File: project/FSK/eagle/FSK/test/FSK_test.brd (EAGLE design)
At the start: 173 x 74 mm, 31 parts, among them IC1 74AUC1G32DCK, X1 SMA-142-0711-821/826, X2 SMA-142-0711-821/826, X3 SMA-142-0711-821/826, X4 SMA-142-0711-821/826, X5 SMA-142-0711-821/826, X6 22-23-2021

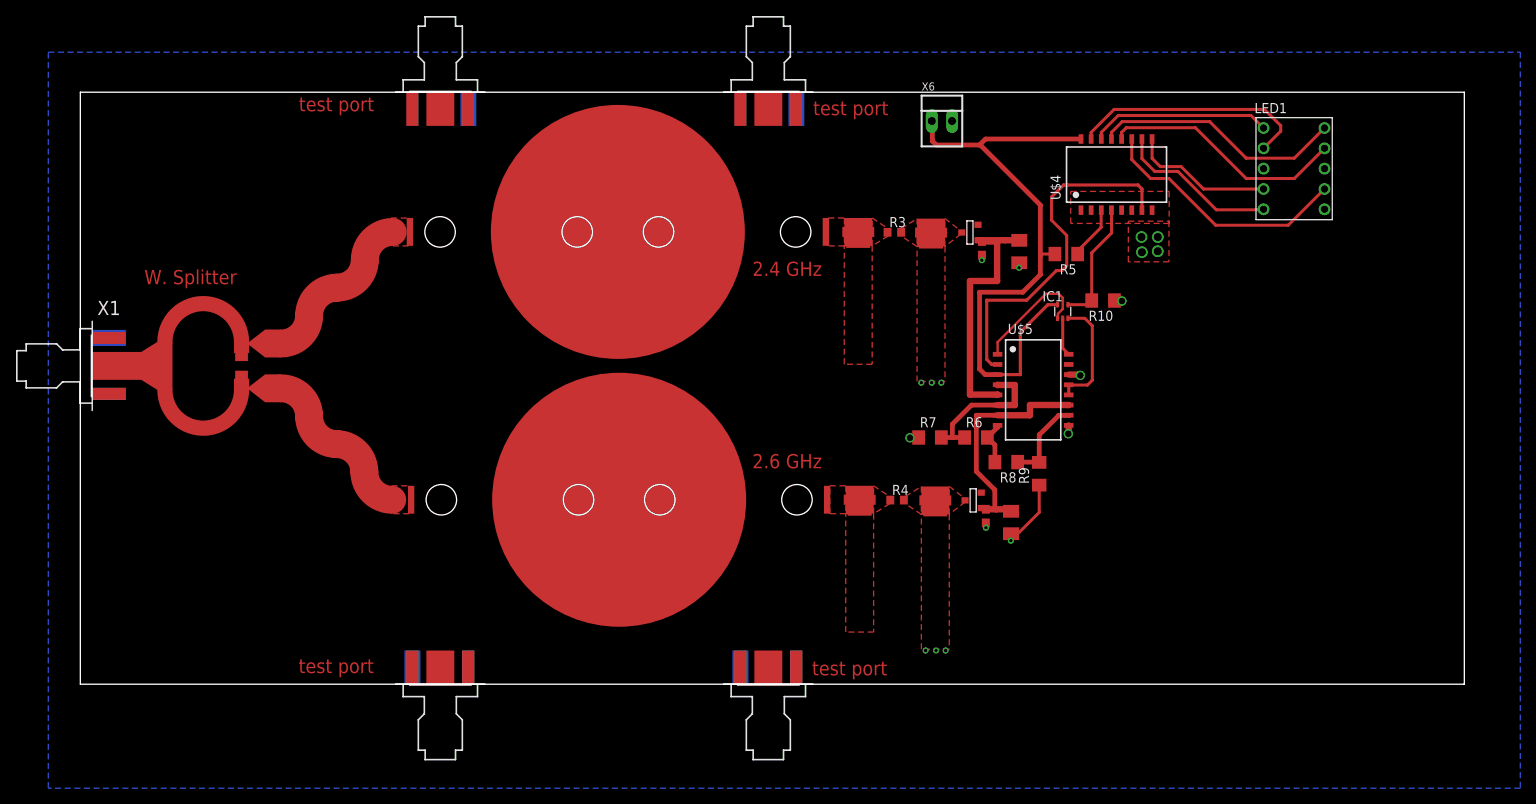
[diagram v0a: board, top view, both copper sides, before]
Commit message: fixed footprints for comp. and  SSD driver
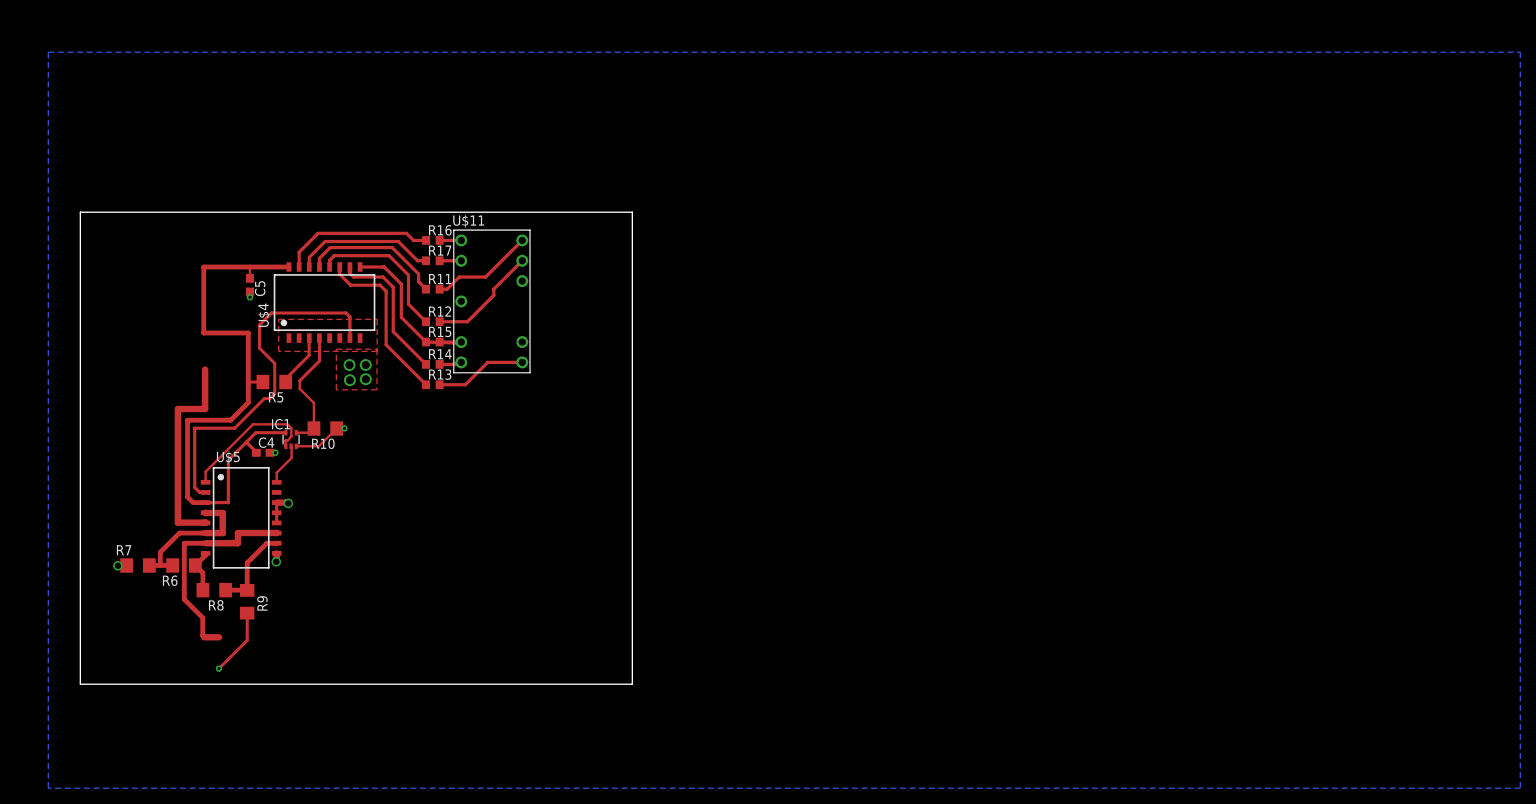
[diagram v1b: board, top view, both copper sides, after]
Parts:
- removed 2.4FIL, 2.4TUNED, 2.6FIL, 2.6TUNED: TEE_TL1, ECE532_Parts:TEE_TL1
- removed C1, C2: 100 pF, rcl:C0603
- removed FILTER1: 2.4GHz, ECE532_Parts:1IN_PIPE_CAP
- removed FILTER2: 2.6GHz, ECE532_Parts:1IN_PIPE_CAP
- removed LED1: S4301B, led-7-segment:S4301B
- removed R1, R2: 10k, rcl:M1206
- removed R3, R4: (no value), rcl:R0603
- removed U$1: WSPLITTER_2.5GHZ, ECE532_Parts:WSPLITTER_2.5GHZ
- removed U$2, U$3: HSMS-2850, ECE532_Parts:HSMS-2850
- removed X1, X2, X3, X4, X5: SMA-142-0711-821/826, con-coax:J502-ND-142-0711-821/826
- removed X6: 22-23-2021, con-molex:22-23-2021
- added C4, C5: (no value), rcl:C0603
- added R11, R12, R13, R14, R15, R16, R17: (no value), rcl:R0603
- added U$11: 7S_DISPLAY, ECE532_Parts:7S_DISPLAY
- moved R5 100.3 mm to (20.2, 35.8)
- moved R6 100.3 mm to (8.96, 12.8)
- moved R7 100.3 mm to (3.21, 12.8)
- moved R8 100.3 mm to (12.7, 9.76)
- moved R9 100.3 mm to (16.9, 8.31)
- moved U$4 100.3 mm to (25.3, 45.7)
- moved U$5 100.3 mm to (16.1, 18.8)
- moved R10 98.5 mm to (26.6, 30.0)
- moved IC1 97.8 mm to (22.3, 28.6)
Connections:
- removed net 2.4FIL: 2.4FIL.T_B, 2.4FIL.T_L, 2.4FIL.T_R, FILTER1.OUT, R3.1
- removed net 2.4GHZ: FILTER1.IN, U$1.P$2
- removed net 2.4TUNED: 2.4TUNED.T_B, 2.4TUNED.T_L, 2.4TUNED.T_R, R3.2, U$2.A
- removed net 2.6FIL: 2.6FIL.T_B, 2.6FIL.T_L, 2.6FIL.T_R, FILTER2.OUT, R4.1
- removed net 2.6GHZ: FILTER2.IN, U$1.P$3
- removed net 2.6TUNED: 2.6TUNED.T_B, 2.6TUNED.T_L, 2.6TUNED.T_R, R4.2, U$3.A
- removed net AGND: IC1.3, U$5.12, U$5.13
- removed net N$5: U$1.P$1, X1.1
- new net N$20: R14.1, U$4.10
- new net N$21: R15.1, U$4.9
- new net N$22: R16.1, U$4.15
- new net N$23: R17.1, U$4.14
- new net N$3: R11.2, U$11.10
- new net N$4: R12.2, U$11.9
- new net N$7: R13.2, U$11.6
- net 2.4_OUT: no longer C1.1, R1.2, U$2.C
- net 2.6_OUT: no longer C2.1, R2.2, U$3.C
- net GND1: now also C4.2, C5.2, IC1.3, U$11.3, U$11.8, U$5.12, U$5.13; no longer C1.2, C2.2, LED1.3, LED1.8, R1.1, R2.1, X1.G@1, X1.G@2, X1.G@3, X1.G@4
- net N$13: now also R14.2, U$11.5; no longer LED1.4, U$4.9
- net N$14: now also R15.2, U$11.4; no longer LED1.5, U$4.10
- net N$15: now also R16.2, U$11.1; no longer LED1.7, U$4.11
- net N$16: now also R17.2, U$11.2; no longer LED1.9, U$4.12
- net N$17: now also R11.1; no longer LED1.10
- net N$18: now also R12.1, U$4.12; no longer LED1.1, U$4.14
- net N$19: now also R13.1, U$4.11; no longer LED1.2, U$4.15
- net VCC: now also C4.1, C5.1; no longer X6.1
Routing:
- net N$15: track 31.9 -> 2.71 mm
- net N$16: track 30.6 -> 2.71 mm
- net N$22: track 0.00 -> 19.1 mm
- net N$21: track 0.00 -> 18.6 mm
- net N$20: track 0.00 -> 18.3 mm
- net N$23: track 0.00 -> 17.6 mm
- net N$14: track 20.3 -> 2.71 mm
- net N$13: track 17.9 -> 2.81 mm
- net AGND: track 14.7 -> 0.00 mm
- net N$4: track 0.00 -> 13.9 mm
- net N$17: track 31.5 -> 17.7 mm
- net N$3: track 0.00 -> 12.9 mm
- net N$7: track 0.00 -> 11.5 mm
- net 2.6GHZ: track 9.87 -> 0.00 mm
- net 2.4GHZ: track 9.87 -> 0.00 mm
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- removed copper zone on layer 1, net 2.4FIL
- removed copper zone on layer 1, net 2.4GHZ
- removed copper zone on layer 1, net 2.4TUNED
- removed copper zone on layer 1, net 2.6FIL
- removed copper zone on layer 1, net 2.6GHZ
- removed copper zone on layer 1, net 2.6TUNED
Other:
- board size 173 x 74 mm -> 69 x 59 mm
- board text removed: "2.4 GHz"
- board text removed: "2.6 GHz"
- board text removed: "W. Splitter"
- board text removed: "test port"
